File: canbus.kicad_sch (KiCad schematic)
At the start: 10 parts, among them U1 MCP2518FD, U2 MCP2562FD, Y1 40 MHz

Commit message: schematic and routing updated
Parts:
- added C4, C6: 1u, Capacitor_SMD:C_0805_2012Metric, symbol Device:C
- renumbered C4 to C1, C5 to C2, C1 to C3, C3 to C5, C2 to C7
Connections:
- net +5V: now also C6.1
- net GND: now also C4.2, C6.2
- net VDD: now also C4.1
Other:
- moved on the sheet: C3, C5, C7

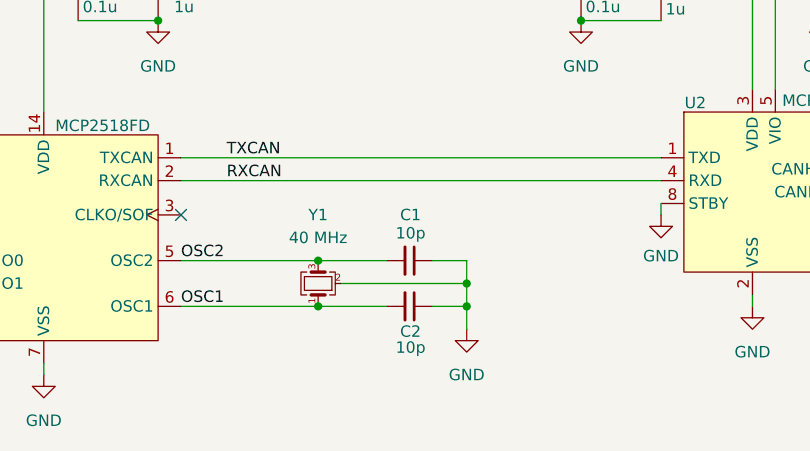
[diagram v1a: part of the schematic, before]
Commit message: Change radio reset pullup to IO voltage, fix net labels
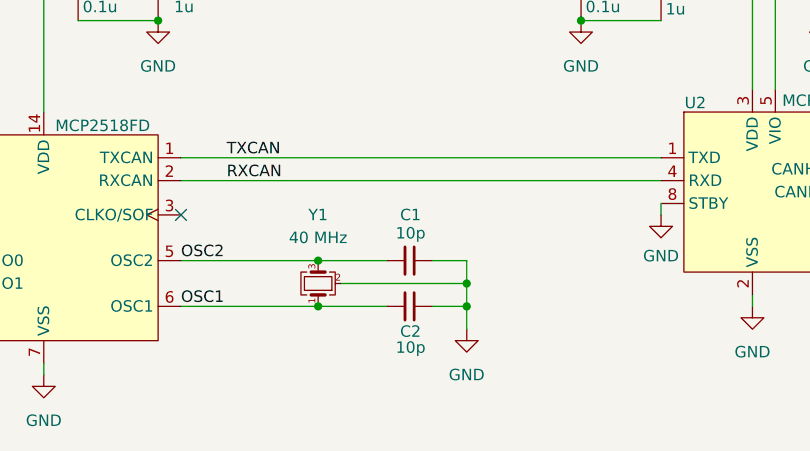
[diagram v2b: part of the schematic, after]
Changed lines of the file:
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@@
 		(title "LEOS CANbus")
 		(date "2026-10-05")
-		(rev "1.0")
+		(rev "2.1")
 		(company "VIP Lightning From the Edge of Space")
 	)
@@
 			)
 		)
-		(property "Description" "10pF 50V C0G/NP0 0805"
+		(property "Description" "Unpolarized capacitor, small symbol"
 			(at 106.68 74.93 0)
 			(hide yes)
@@
 			)
 		)
-		(property "Description" "10pF 50V C0G/NP0 0805"
+		(property "Description" "Unpolarized capacitor, small symbol"
 			(at 106.68 80.01 0)
 			(hide yes)
